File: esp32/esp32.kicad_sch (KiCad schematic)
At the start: 24 parts, among them J1 Conn_01x06_Pin, J2 Conn_01x06_Pin, J4 Conn_01x06_Pin, J5 USB_C_Receptacle_USB2.0_14P, Q1 MMSS8050, Q2 MMSS8050, SW1 XUNPU TS-1088R-02526, U1 SPX3819M5-L-3-3, U2 CP2102N-Axx-xQFN28

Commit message: update with kicad 8
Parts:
- Q1, Q2: footprint Package_TO_SOT_SMD_AKL:SOT-23 -> Package_TO_SOT_SMD:SOT-23
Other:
- moved on the sheet: C5, R10, SW1

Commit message: esp32: fix reset button
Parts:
- removed R10: 470, Resistor_SMD:R_0603_1608Metric, symbol Device:R
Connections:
- net EN: now also C5.2, SW1.2
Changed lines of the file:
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@@
 	)
 	(junction
-		(at 144.018 143.51)
+		(at 153.416 25.146)
 		(diameter 0)
 		(color 0 0 0 0)
 	)
 	(junction
-		(at 153.416 25.146)
+		(at 124.714 56.134)
 		(diameter 0)
 		(color 0 0 0 0)
 	)
 	(junction
-		(at 124.714 56.134)
+		(at 117.856 63.754)
 		(diameter 0)
 		(color 0 0 0 0)
 	)
 	(junction
-		(at 117.856 63.754)
+		(at 144.018 143.51)
 		(diameter 0)
 		(color 0 0 0 0)
@@
 	(wire
 		(pts
-			(xy 154.686 143.51) (xy 158.75 143.51)
-		)
-		(stroke
-			(width 0)
-			(type default)
-		)
-	)
-	(wire
-		(pts
 			(xy 130.048 25.146) (xy 141.986 25.146)
 		)
@@
 	(wire
 		(pts
-			(xy 144.018 143.51) (xy 147.066 143.51)
-		)
-		(stroke
-			(width 0)
-			(type default)
-		)
-	)
-	(wire
-		(pts
 			(xy 112.776 56.134) (xy 124.714 56.134)
 		)
@@
 	(wire
 		(pts
+			(xy 144.018 143.51) (xy 152.4 143.51)
+		)
+		(stroke
+			(width 0)
+			(type default)
+		)
+	)
+	(wire
+		(pts
 			(xy 117.856 63.754) (xy 124.714 63.754)
 		)
@@
 	)
 	(label "EN"
-		(at 158.75 143.51 0)
+		(at 152.4 143.51 0)
 		(fields_autoplaced yes)
 		(effects
@@
 					(unit 1)
 				)
-			)
-		)
-	)
-	(symbol
-		(lib_id "Device:R")
-		(at 150.876 143.51 90)
-		(unit 1)
-		(exclude_from_sim no)
-		(in_bom yes)
-		(on_board yes)
-		(dnp no)
-		(fields_autoplaced yes)
-		(property "Reference" "R10"
-			(at 150.876 137.16 90)
-			(effects
-				(font
-					(size 1.27 1.27)
-				)
-			)
-		)
-		(property "Value" "470"
-			(at 150.876 139.7 90)
-			(effects
-				(font
-					(size 1.27 1.27)
-				)
-			)
-		)
-		(property "Footprint" "Resistor_SMD:R_0603_1608Metric"
-			(at 150.876 145.288 90)
-			(effects
-				(font
-					(size 1.27 1.27)
-				)
-				(hide yes)
-			)
-		)
-		(property "Datasheet" "~"
-			(at 150.876 143.51 0)
-			(effects
-				(font
-					(size 1.27 1.27)
-				)
-				(hide yes)
-			)
-		)
-		(property "Description" ""
-			(at 150.876 143.51 0)
-			(effects
-				(font
-					(size 1.27 1.27)
-				)
-				(hide yes)
-			)
-		)
-		(pin "2"
-		)
-		(pin "1"
-		)
-		(instances
-			(project "esp32"
-				(path "/2404e350-49a9-4013-9f27-301bc752cce8"
-					(reference "R10")
-					(unit 1)
-				)

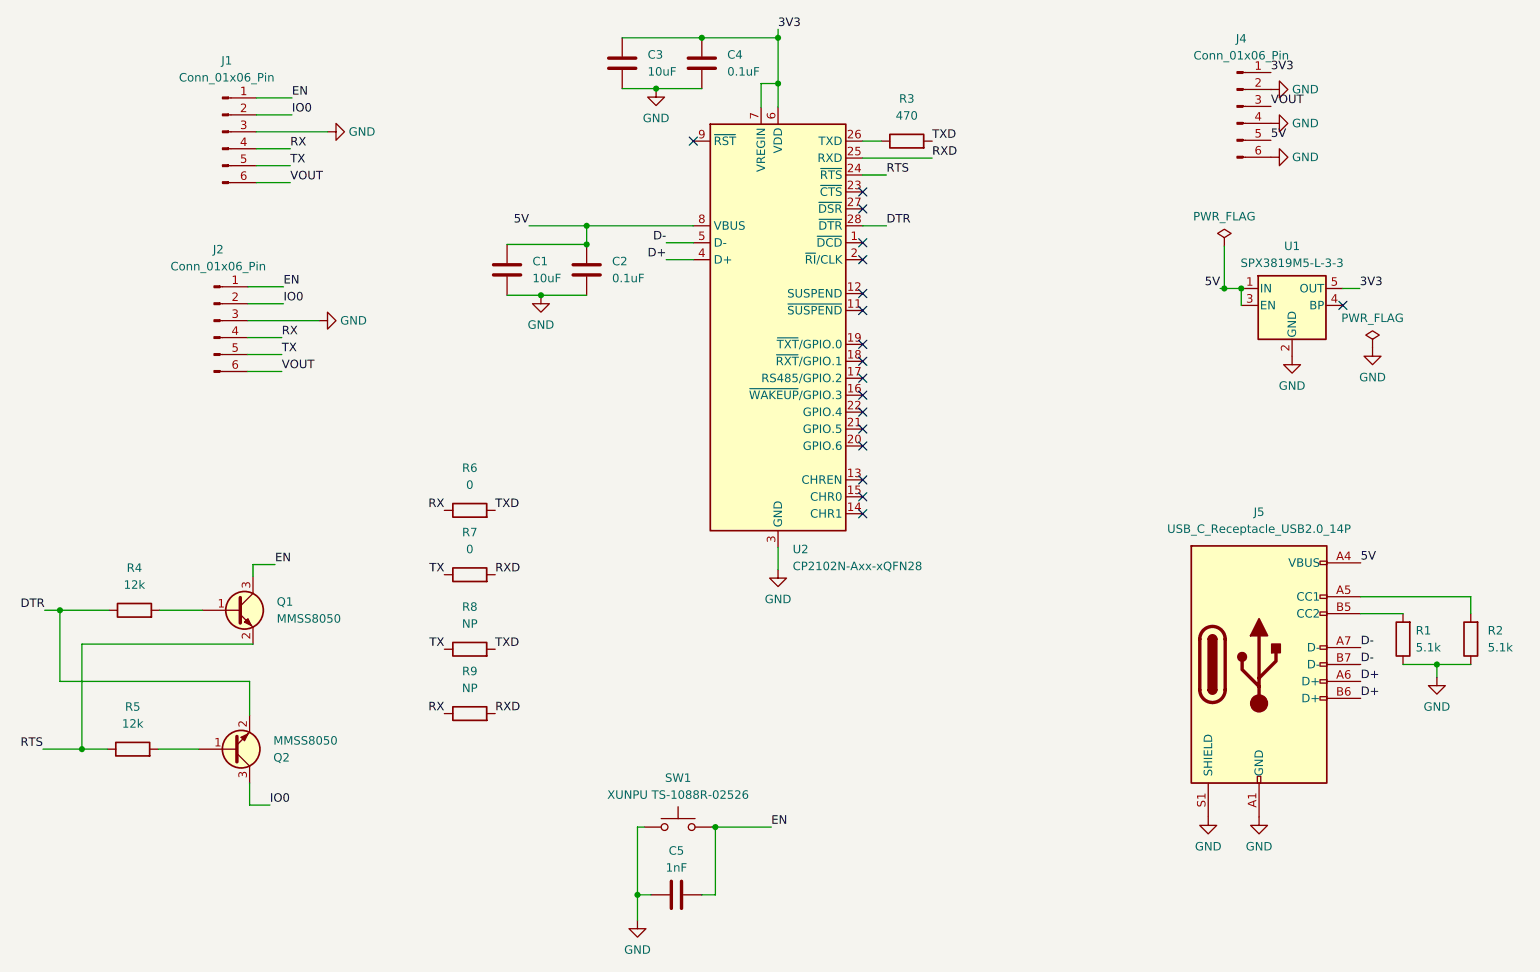
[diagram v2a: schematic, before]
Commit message: esp32: remove R on TX
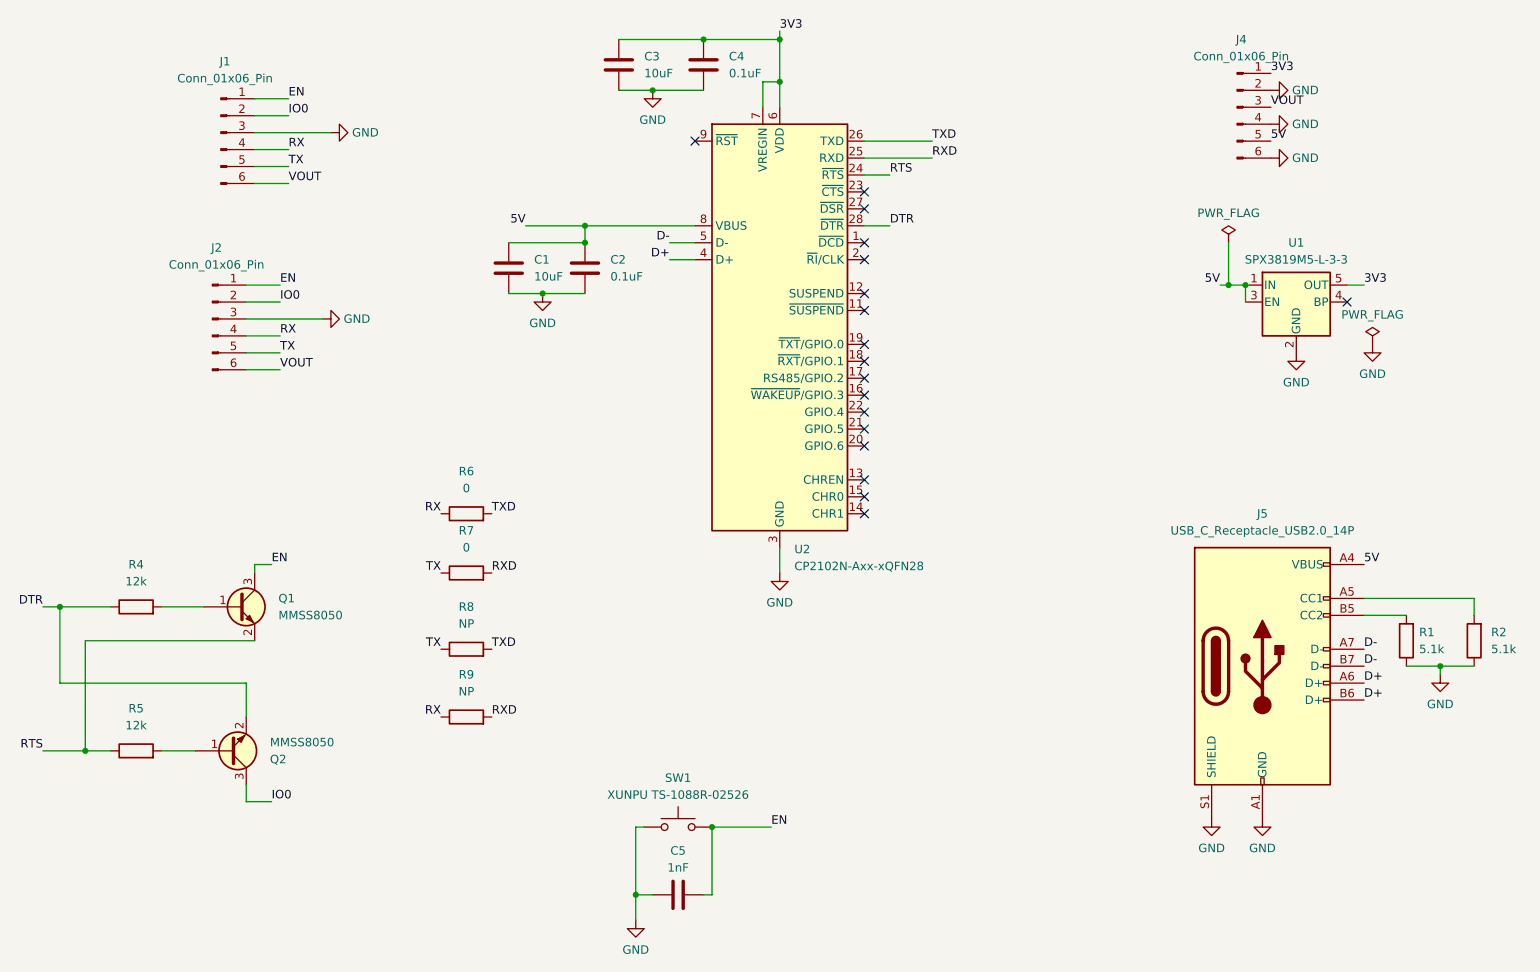
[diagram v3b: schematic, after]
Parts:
- removed R3: 470, Resistor_SMD:R_0603_1608Metric, symbol Device:R
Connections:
- net TXD: now also U2.26 (TXD)
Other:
- moved on the sheet: C3, J5, Q1, Q2, R1, R2, R4, R5, R6, R7, R8, R9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
